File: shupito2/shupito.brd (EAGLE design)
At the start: 41.9 x 23.5 mm, 92 parts, among them IC2 74LVC1T45, IC3 74LVC1T45, IC4 74LVC1T45, IC5 74LVC1T45, IC6 ATXMEGA32A4U-AU, IC7 TPS73033DBV, Q1 BC807W-1907646, Q10 1758094, Q11 PDTC123YU-1757992, Q2 NX2301P-1894738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

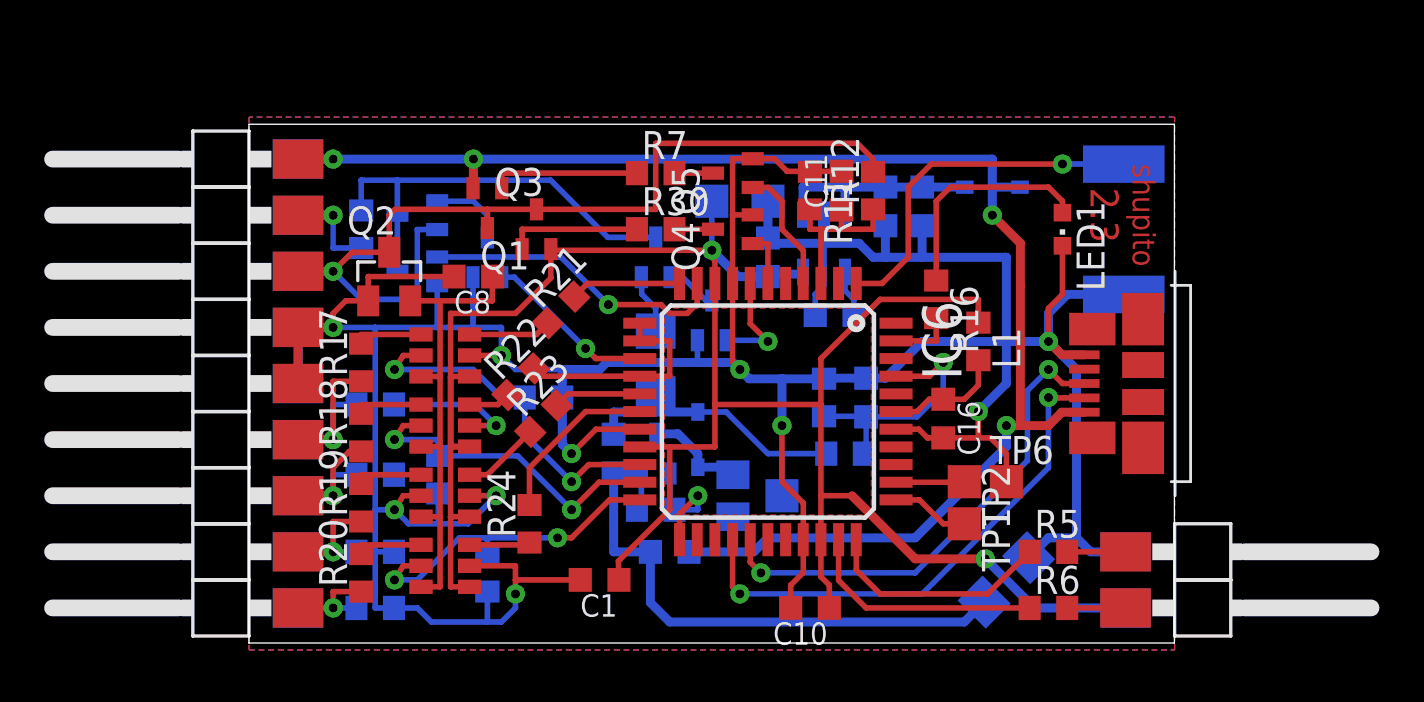
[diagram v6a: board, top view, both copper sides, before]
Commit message: Increased drill size to 0.5mm.
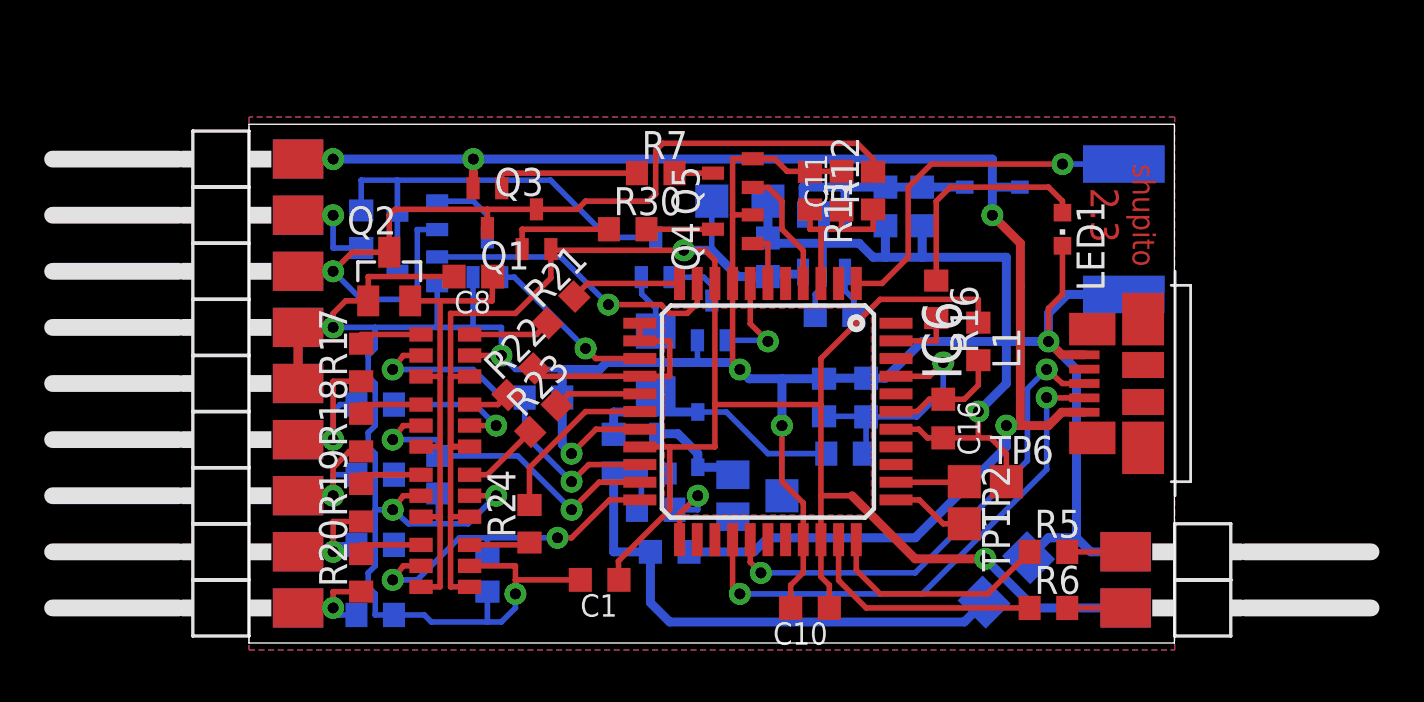
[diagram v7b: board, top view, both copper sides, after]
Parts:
- moved R30 1.27 mm to (17.1, 19.1)
- moved R29 0.32 mm to (5.71, 1.59)
- moved R28 0.32 mm to (5.71, 4.76)
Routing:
- net N$28: track 6.41 -> 4.83 mm
- net N$26: track 1.74 -> 3.01 mm
- net GND: track 200.7 -> 201.7 mm
- net VCC: track 101.6 -> 102.6 mm
- net VCCIO: track 42.9 -> 42.3 mm

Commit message: Added a part name.
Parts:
- Q10: value 1758094 -> PMF280UN,115-1758094
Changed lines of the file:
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@@
 <layer number="23" name="tOrigins" color="15" fill="1" visible="yes" active="yes"/>
 <layer number="24" name="bOrigins" color="15" fill="1" visible="yes" active="yes"/>
-<layer number="25" name="tNames" color="7" fill="1" visible="no" active="yes"/>
-<layer number="26" name="bNames" color="7" fill="1" visible="no" active="yes"/>
+<layer number="25" name="tNames" color="7" fill="1" visible="yes" active="yes"/>
+<layer number="26" name="bNames" color="7" fill="1" visible="yes" active="yes"/>
 <layer number="27" name="tValues" color="7" fill="1" visible="no" active="yes"/>
 <layer number="28" name="bValues" color="7" fill="1" visible="no" active="yes"/>
@@
 <element name="C13" library="rcl" package="C0603K" value="1u/25V-1759039" x="16.51" y="8.89" rot="MR270"/>
 <element name="D2" library="diode" package="SOD323" value="BAT42WS-1621831" x="20.32" y="9.525" rot="MR270"/>
-<element name="Q10" library="transistors" package="SOT323" value="1758094" x="18.415" y="8.89" rot="MR0"/>
+<element name="Q10" library="transistors" package="SOT323" value="PMF280UN,115-1758094" x="18.415" y="8.89" rot="MR0"/>
 <element name="R1" library="rcl" package="R0603" value="330" x="5.08" y="19.05" rot="MR270"/>
 <element name="R2" library="rcl" package="R0603" value="6k8" x="18.415" y="6.35" rot="MR0"/>
